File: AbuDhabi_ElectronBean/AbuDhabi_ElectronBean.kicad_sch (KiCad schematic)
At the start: 12 parts, among them J12 Sensor, J13 Bomba, J14 Eingang - obere Pins, J15 Eingang - obere Pins, J16 Power, J17 Control, J18 Data

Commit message: Arduino Mega footpring change and LEDs addition
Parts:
- added D1, D3, D4: LED, LED_SMD:LED_0603_1608Metric_Pad1.05x0.95mm_HandSolder, symbol Device:LED
- added J21: Versorgung(opt), Connector_JST:JST_EH_B4B-EH-A_1x04_P2.50mm_Vertical, symbol Connector:Conn_01x04_Female
- added R1, R3, R4: 220, Resistor_SMD:R_0805_2012Metric_Pad1.20x1.40mm_HandSolder, symbol Device:R
- A3: footprint Arduino:Footprint_Mega2560_Pro_Socket -> Arduino:Arduino_Mega2560_R3_Shield
- J20: value (none) -> MUX_output; footprint (none) -> Connector_JST:JST_EH_B4B-EH-A_1x04_P2.50mm_Vertical
- U1: value (none) -> 74HC139P; footprint (none) -> Package_DIP:DIP-16_W7.62mm
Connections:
- net 5V is gone; now on net 5VExt: J16.2 (Pin_2)
- net GND Ard is gone; now on net GND: J16.1 (Pin_1)
- net GND ext is gone; now on net GND: J12.1 (Pin_1), J13.1 (Pin_1)
- net Rx1 is gone; now on net Rx3: A2.15 (D0/RX)
- net Tx1 is gone; now on net Tx3: A2.16 (D1/TX)
- net 5VExt: now also D1.2 (A), J21.4 (Pin_4)
- net 5Vard: now also D3.2 (A)
- net GND: now also J21.1 (Pin_1), J21.2 (Pin_2), R1.2, R3.2, R4.2
- net IO5: now also A3.D5
- net 3.3V renamed +3.3V
- net +3.3V: now also D4.2 (A), J21.3 (Pin_3)
- new net: D4.1 (K), R4.1
- new net: D1.1 (K), R1.1
- new net: D3.1 (K), R3.1
- no-connect marks 123 -> 122
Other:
- note added: "LEDs 2.0"
- moved on the sheet: J16, J17, J18

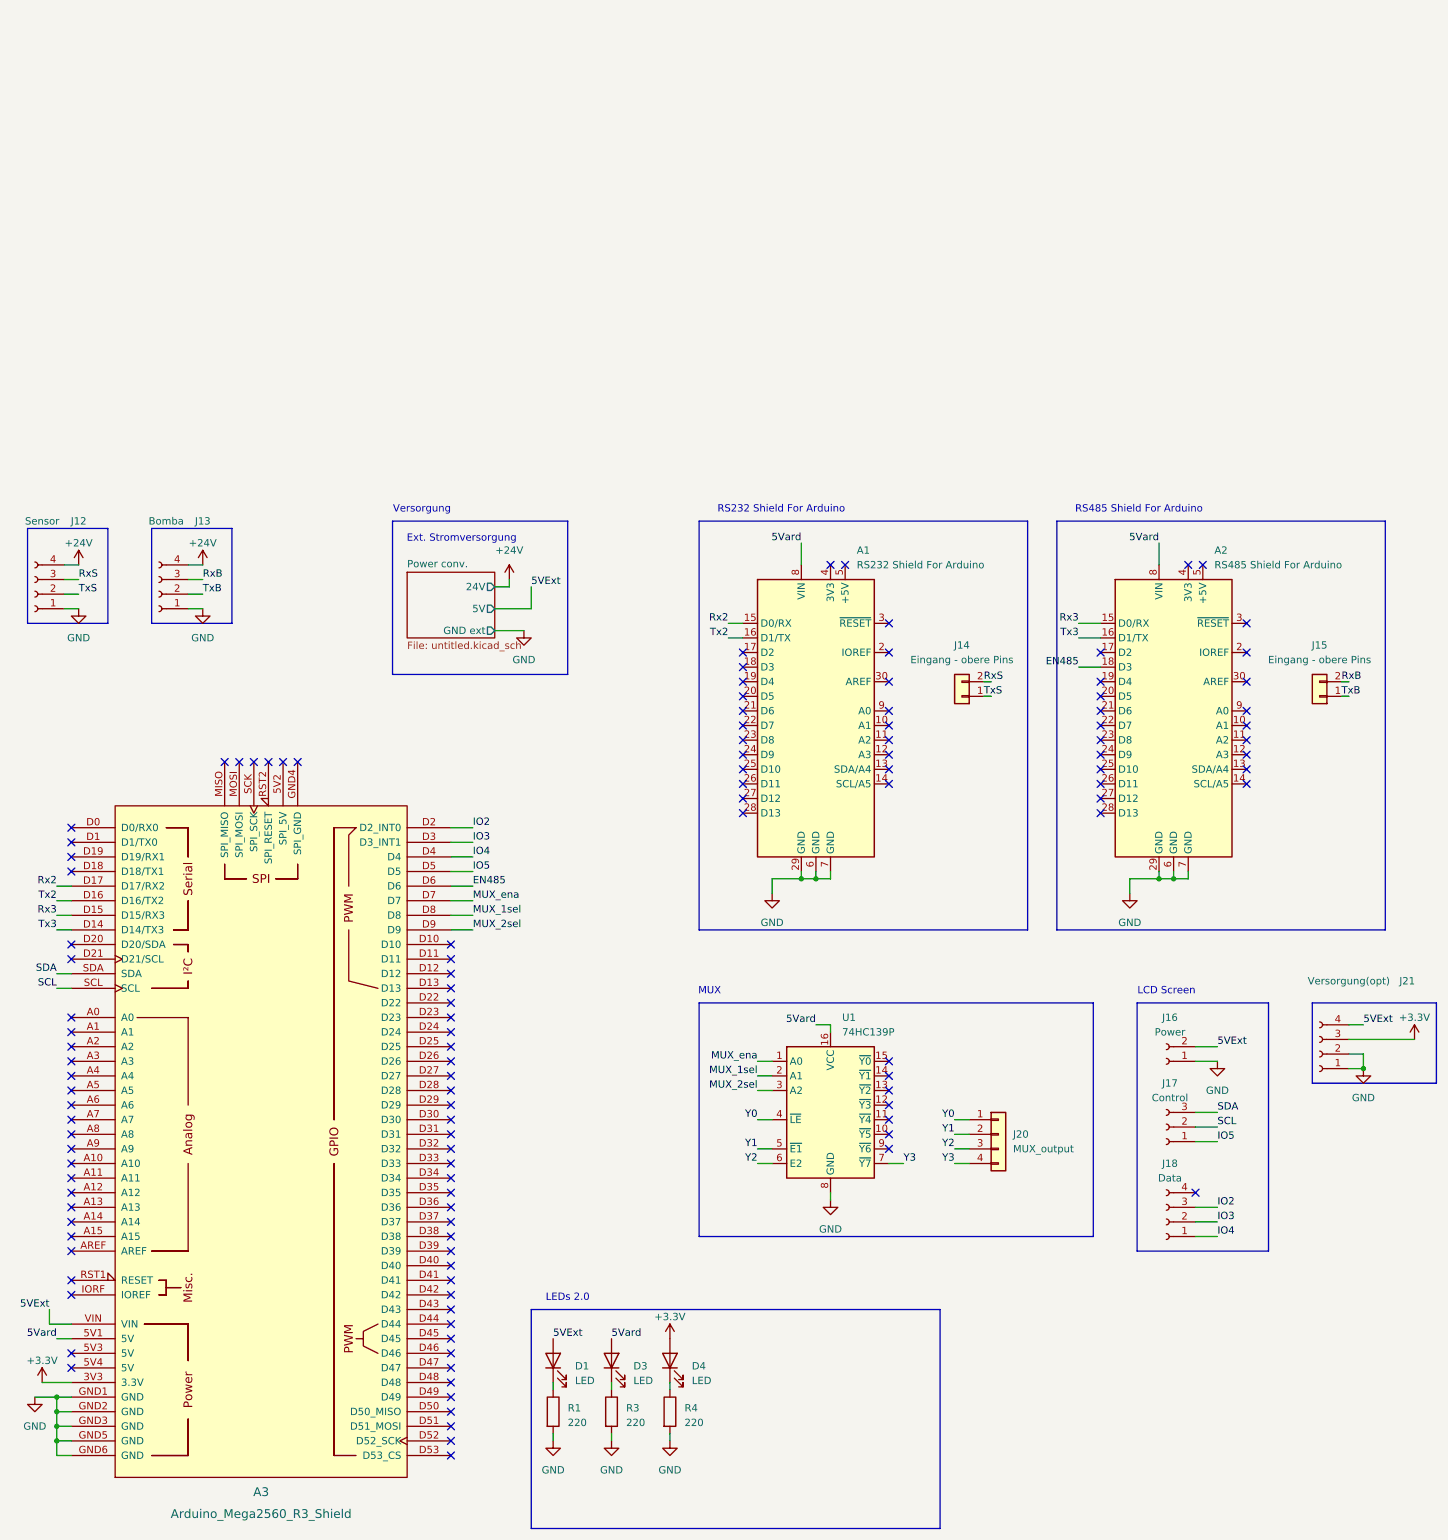
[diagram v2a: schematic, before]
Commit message: RS232 und RS435 shields entfernt
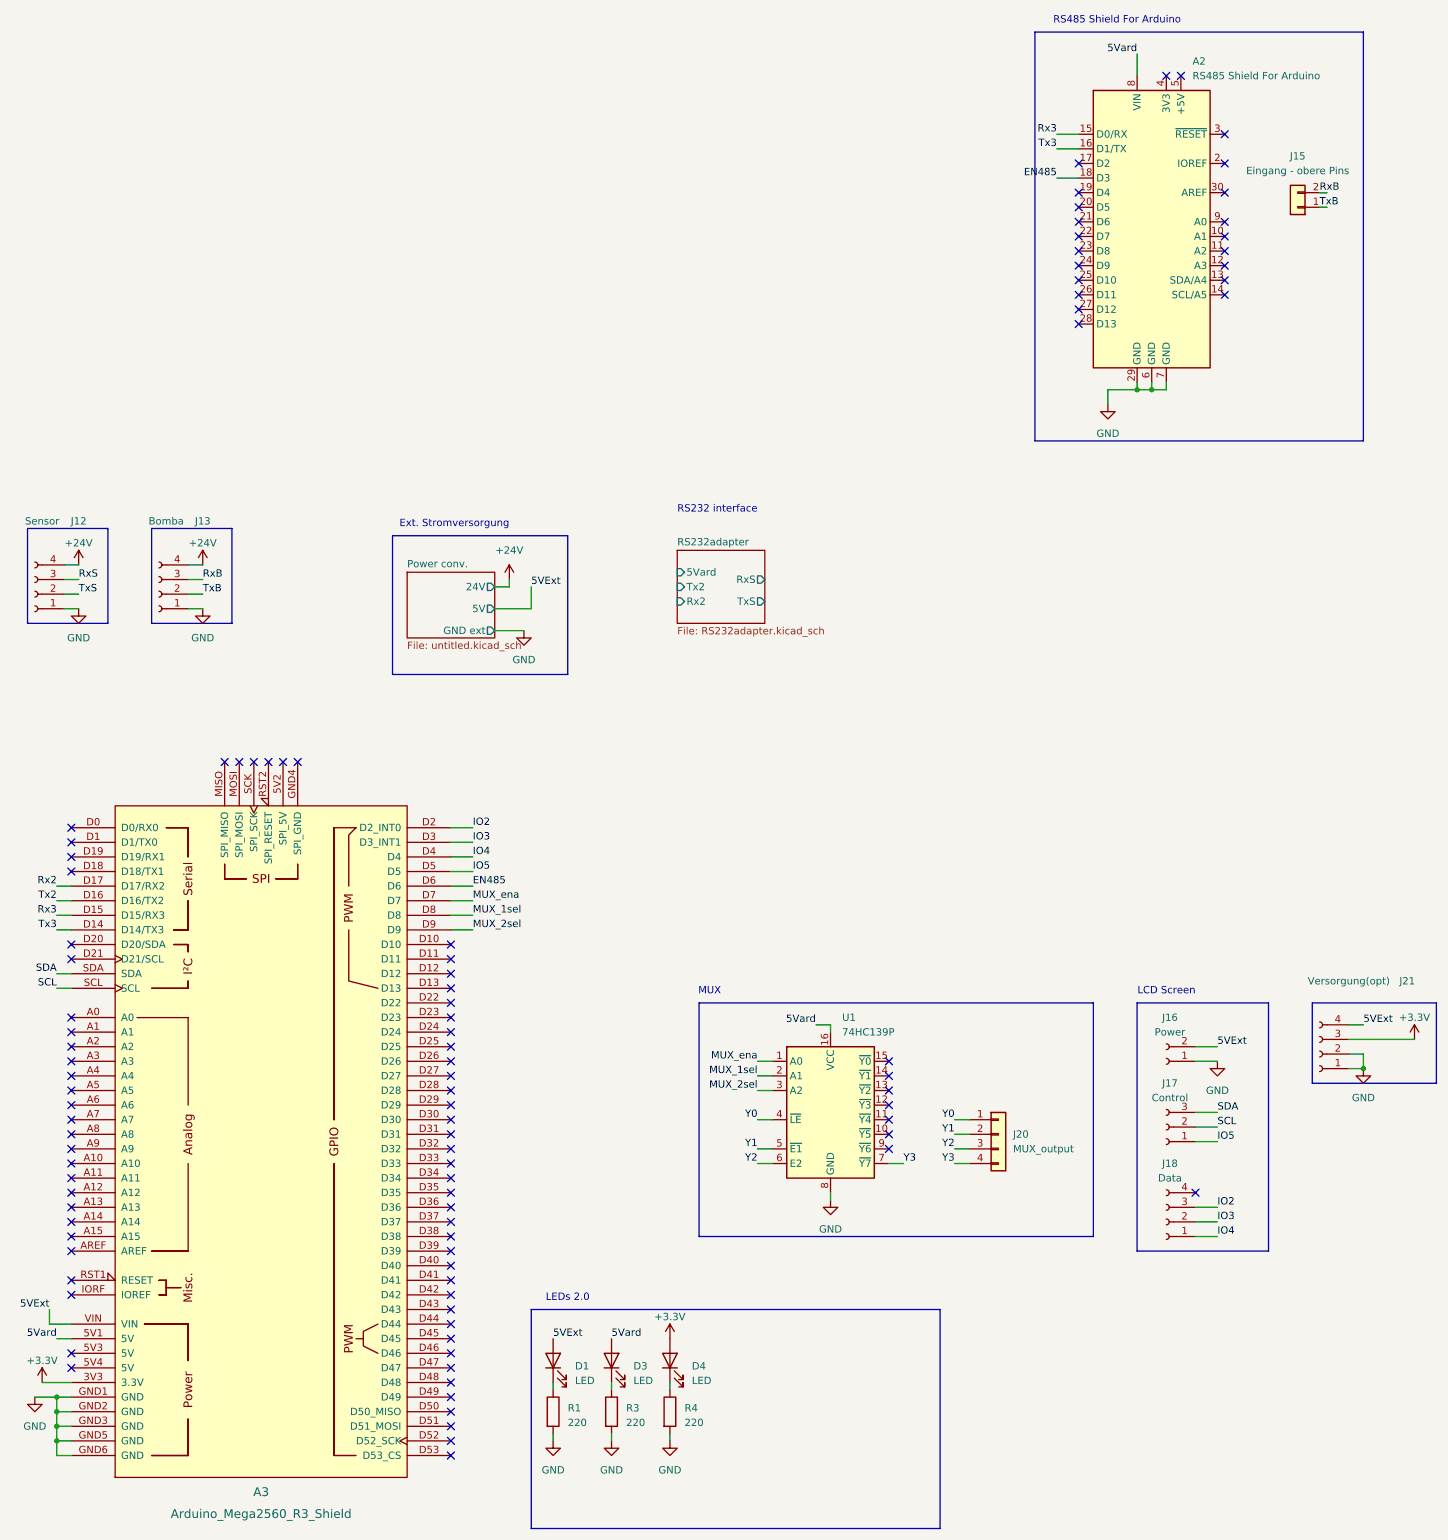
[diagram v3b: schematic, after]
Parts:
- removed A1: RS232 Shield For Arduino, Module:Arduino_UNO_R2, symbol MCU_Module:Arduino_UNO_R2
- removed J14: Eingang - obere Pins, Connector_JST:JST_EH_B2B-EH-A_1x02_P2.50mm_Vertical, symbol Connector_Generic:Conn_01x02
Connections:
- no-connect marks 122 -> 99
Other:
- added sheet RS232adapter (RS232adapter.kicad_sch)
- note added: "RS232 interface"
- note removed: "RS232 Shield For Arduino"
- note removed: "Versorgung"
- moved on the sheet: A2, J15

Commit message: RS435 interface start
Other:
- added sheet RS435adapter (RS435adapter.kicad_sch)
- note added: "RS435 interface"
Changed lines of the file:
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@@
+    (stroke (width 0) (type default))
+  )
+  (wire (pts (xy 128.27 35.56) (xy 129.54 35.56))
     (stroke (width 0) (type default))
   )
@@
     (stroke (width 0) (type default))
   )
+  (polyline (pts (xy 121.92 21.59) (xy 161.29 21.59))
+    (stroke (width 0) (type default))
+  )
   (polyline (pts (xy 240.03 102.87) (xy 261.62 102.87))
     (stroke (width 0) (type default))
@@
     (stroke (width 0) (type default))
   )
+  (polyline (pts (xy 121.92 21.59) (xy 121.92 43.18))
+    (stroke (width 0) (type default))
+  )
   (wire (pts (xy 177.8 123.19) (xy 180.34 123.19))
     (stroke (width 0) (type default))
@@
     (stroke (width 0) (type default))
   )
+  (wire (pts (xy 144.78 31.75) (xy 147.32 31.75))
+    (stroke (width 0) (type default))
+  )
   (wire (pts (xy 209.55 -3.81) (xy 204.47 -3.81))
     (stroke (width 0) (type default))
   )
+  (wire (pts (xy 128.27 33.02) (xy 129.54 33.02))
+    (stroke (width 0) (type default))
+  )
   (wire (pts (xy 90.17 80.01) (xy 93.98 80.01))
     (stroke (width 0) (type default))
@@
     (stroke (width 0) (type default))
   )
+  (wire (pts (xy 128.27 30.48) (xy 129.54 30.48))
+    (stroke (width 0) (type default))
+  )
   (wire (pts (xy 21.59 82.55) (xy 24.13 82.55))
     (stroke (width 0) (type default))
@@
     (stroke (width 0) (type default))
   )
+  (polyline (pts (xy 161.29 21.59) (xy 161.29 43.18))
+    (stroke (width 0) (type default))
+  )
   (polyline (pts (xy 104.14 156.21) (xy 175.26 156.21))
     (stroke (width 0) (type default))
@@
     (stroke (width 0) (type default))
   )
+  (polyline (pts (xy 161.29 43.18) (xy 121.92 43.18))
+    (stroke (width 0) (type default))
+  )
   (polyline (pts (xy 175.26 194.31) (xy 175.26 156.21))
     (stroke (width 0) (type default))
@@
     (stroke (width 0) (type default))
   )
+  (wire (pts (xy 144.78 35.56) (xy 147.32 35.56))
+    (stroke (width 0) (type default))
+  )
   (polyline (pts (xy 191.77 -66.04) (xy 248.92 -66.04))
     (stroke (width 0) (type default))
@@
     (stroke (width 0) (type default))
   )
+  (text "RS435 interface" (at 184.15 20.32 0)
+    (effects (font (size 1.27 1.27)) (justify right bottom))
+  )
   (text "LCD Screen" (at 219.71 101.6 0)
     (effects (font (size 1.27 1.27)) (justify right bottom))
@@
     (effects (font (size 1.27 1.27)) (justify right bottom))
   )
-  (text "RS232 interface" (at 143.51 17.78 0)
+  (text "RS232 interface" (at 137.16 20.32 0)
     (effects (font (size 1.27 1.27)) (justify right bottom))
   )
@@
     (effects (font (size 1.27 1.27)) (justify left bottom))
   )
+  (label "Rx2" (at 128.27 35.56 180) (fields_autoplaced)
+    (effects (font (size 1.27 1.27)) (justify right bottom))
+  )
   (label "Y0" (at 177.8 123.19 180) (fields_autoplaced)
     (effects (font (size 1.27 1.27)) (justify right bottom))
@@
     (effects (font (size 1.27 1.27)) (justify left bottom))
   )
+  (label "5Vard" (at 128.27 30.48 180) (fields_autoplaced)
+    (effects (font (size 1.27 1.27)) (justify right bottom))
+  )
   (label "SCL" (at 21.59 100.33 180) (fields_autoplaced)
     (effects (font (size 1.27 1.27)) (justify right bottom))
@@
     (effects (font (size 1.27 1.27)) (justify left bottom))
   )
+  (label "TxS" (at 147.32 35.56 0) (fields_autoplaced)
+    (effects (font (size 1.27 1.27)) (justify left bottom))
+  )
   (label "Y2" (at 143.51 130.81 180) (fields_autoplaced)
     (effects (font (size 1.27 1.27)) (justify right bottom))
@@
     (effects (font (size 1.27 1.27)) (justify left bottom))
   )
+  (label "RxS" (at 147.32 31.75 0) (fields_autoplaced)
+    (effects (font (size 1.27 1.27)) (justify left bottom))
+  )
   (label "IO5" (at 93.98 80.01 0) (fields_autoplaced)
     (effects (font (size 1.27 1.27)) (justify left bottom))
@@
   )
   (label "MUX_1sel" (at 143.51 115.57 180) (fields_autoplaced)
+    (effects (font (size 1.27 1.27)) (justify right bottom))
+  )
+  (label "Tx2" (at 128.27 33.02 180) (fields_autoplaced)
     (effects (font (size 1.27 1.27)) (justify right bottom))
   )
@@
     )
   )
+  (sheet (at 176.53 26.67) (size 15.24 12.7) (fields_autoplaced)
+    (stroke (width 0.1524) (type solid))
+    (fill (color 0 0 0 0.0000))
+    (property "Sheetname" "RS435adapter" (at 176.53 25.9584 0)
+      (effects (font (size 1.27 1.27)) (justify left bottom))
+    )
+    (property "Sheetfile" "RS435adapter.kicad_sch" (at 176.53 39.9546 0)
+      (effects (font (size 1.27 1.27)) (justify left top))
+    )
+    (instances
+      (project "AbuDhabi_ElectronBean"
+        (path "/e63e39d7-6ac0-4ffd-8aa3-1841a4541b55" (page "4"))
+      )
+    )
+  )
   (sheet (at 82.55 27.94) (size 15.24 11.43) (fields_autoplaced)
     (stroke (width 0.1524) (type solid))
@@
     )
   )
-  (sheet (at 129.54 24.13) (size 15.24 12.7) (fields_autoplaced)
+  (sheet (at 129.54 26.67) (size 15.24 12.7) (fields_autoplaced)
     (stroke (width 0.1524) (type solid))
     (fill (color 0 0 0 0.0000))
-    (property "Sheetname" "RS232adapter" (at 129.54 23.4184 0)
+    (property "Sheetname" "RS232adapter" (at 129.54 25.9584 0)
       (effects (font (size 1.27 1.27)) (justify left bottom))
     )
-    (property "Sheetfile" "RS232adapter.kicad_sch" (at 129.54 37.4146 0)
+    (property "Sheetfile" "RS232adapter.kicad_sch" (at 129.54 39.9546 0)
       (effects (font (size 1.27 1.27)) (justify left top))
     )
-    (pin "5Vard" input (at 129.54 27.94 180)
-      (effects (font (size 1.27 1.27)) (justify left))
-    )
-    (pin "Tx2" input (at 129.54 30.48 180)
-      (effects (font (size 1.27 1.27)) (justify left))
-    )
-    (pin "Rx2" input (at 129.54 33.02 180)
-      (effects (font (size 1.27 1.27)) (justify left))
-    )
-    (pin "RxS" output (at 144.78 29.21 0)
+    (pin "5Vard" input (at 129.54 30.48 180)
+      (effects (font (size 1.27 1.27)) (justify left))
+    )
+    (pin "Tx2" input (at 129.54 33.02 180)
+      (effects (font (size 1.27 1.27)) (justify left))
+    )
+    (pin "Rx2" input (at 129.54 35.56 180)
+      (effects (font (size 1.27 1.27)) (justify left))
+    )
+    (pin "RxS" output (at 144.78 31.75 0)
       (effects (font (size 1.27 1.27)) (justify right))
     )
-    (pin "TxS" output (at 144.78 33.02 0)
+    (pin "TxS" output (at 144.78 35.56 0)
       (effects (font (size 1.27 1.27)) (justify right))
     )
